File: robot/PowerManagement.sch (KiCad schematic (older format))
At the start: 13 parts

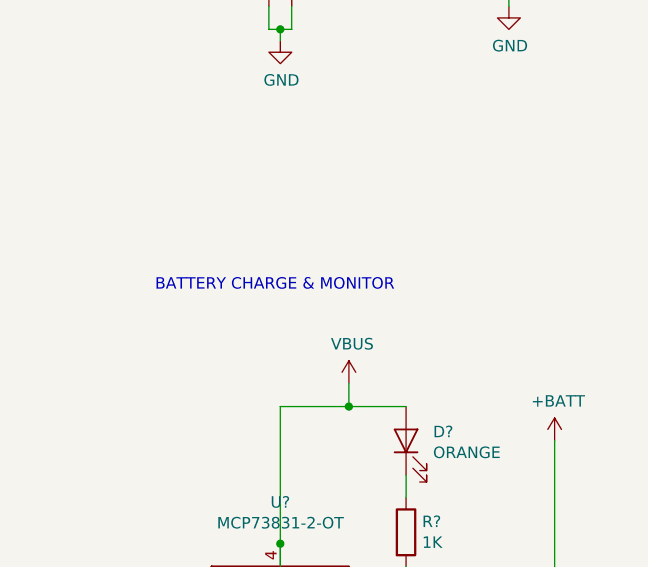
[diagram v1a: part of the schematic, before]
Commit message: UI parts, (re)wiring remaining signals
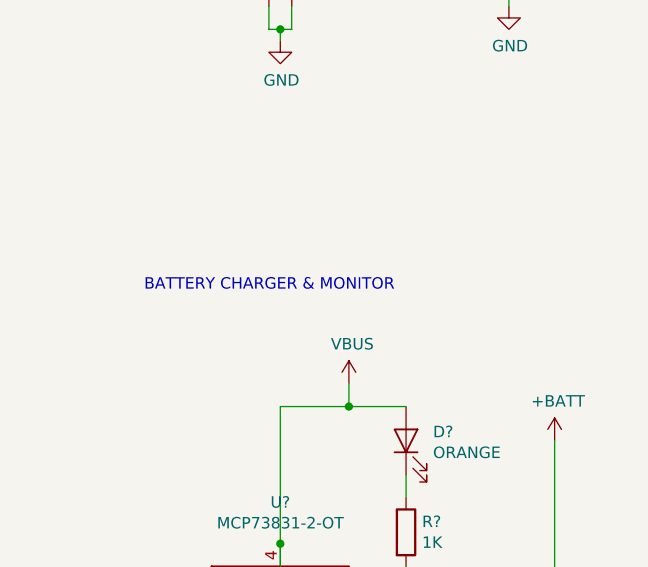
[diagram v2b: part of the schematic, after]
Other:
- note added: "BATTERY CHARGER & MONITOR"
- note removed: "BATTERY CHARGE & MONITOR"
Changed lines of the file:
@@
 $Descr A4 11693 8268
 encoding utf-8
-Sheet 2 7
+Sheet 2 8
 Title "Micro Sumo: Power Management"
 Date "2019-06-28"
@@
 BAT_MON
 Text Notes 3500 3850 2    50   ~ 0
-BATTERY CHARGE & MONITOR
+BATTERY CHARGER & MONITOR
 $Comp
 L dk_PMIC-Voltage-Regulators-Linear:LD1117S33CTR U?

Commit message: DRC check fixes and small changes
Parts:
- gave numbers to parts that had none: 13
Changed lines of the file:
@@
 $EndDescr
 $Comp
-L Battery_Management:MCP73831-2-OT U?
+L Battery_Management:MCP73831-2-OT U2
 U 1 1 5D163C93
 P 3000 5250
-F 0 "U?" H 3000 5731 50  0000 C CNN
+F 0 "U2" H 3000 5731 50  0000 C CNN
 F 1 "MCP73831-2-OT" H 3000 5640 50  0000 C CNN
 F 2 "Package_TO_SOT_SMD:SOT-23-5" H 3050 5000 50  0001 L CIN
@@
 $EndComp
 $Comp
-L Device:R R?
+L Device:R R4
 U 1 1 5D167CB7
 P 2500 5700
-F 0 "R?" H 2570 5746 50  0000 L CNN
+F 0 "R4" H 2570 5746 50  0000 L CNN
 F 1 "5K" H 2570 5655 50  0000 L CNN
 F 2 "" V 2430 5700 50  0001 C CNN
@@
 $EndComp
 $Comp
-L Device:C C?
+L Device:C C2
 U 1 1 5D16C2F0
 P 4200 5350
-F 0 "C?" H 4315 5396 50  0000 L CNN
+F 0 "C2" H 4315 5396 50  0000 L CNN
 F 1 "10µ" H 4315 5305 50  0000 L CNN
 F 2 "" H 4238 5200 50  0001 C CNN
@@
 	3300 4350 3300 4250
 $Comp
-L Device:LED D?
+L Device:LED D2
 U 1 1 5D16DD5D
 P 3550 4500
-F 0 "D?" V 3589 4382 50  0000 R CNN
+F 0 "D2" V 3589 4382 50  0000 R CNN
 F 1 "ORANGE" V 3498 4382 50  0000 R CNN
 F 2 "" H 3550 4500 50  0001 C CNN
@@
 Connection ~ 3300 4350
 $Comp
-L Device:R R?
+L Device:R R3
 U 1 1 5D170C73
 P 3550 4900
-F 0 "R?" H 3620 4946 50  0000 L CNN
+F 0 "R3" H 3620 4946 50  0000 L CNN
 F 1 "1K" H 3620 4855 50  0000 L CNN
 F 2 "" V 3480 4900 50  0001 C CNN
@@
 	3400 5150 4200 5150
 $Comp
-L Device:R R?
+L Device:R R1
 U 1 1 5D176A1F
 P 7650 1850
-F 0 "R?" H 7720 1896 50  0000 L CNN
+F 0 "R1" H 7720 1896 50  0000 L CNN
 F 1 "100K" H 7720 1805 50  0000 L CNN
 F 2 "" V 7580 1850 50  0001 C CNN
@@
 $EndComp
 $Comp
-L Device:R R?
+L Device:R R2
 U 1 1 5D176E0F
 P 7650 2350
-F 0 "R?" H 7720 2396 50  0000 L CNN
+F 0 "R2" H 7720 2396 50  0000 L CNN
 F 1 "100K" H 7720 2305 50  0000 L CNN
 F 2 "" V 7580 2350 50  0001 C CNN
@@
 BATTERY CHARGER & MONITOR
 $Comp
-L dk_PMIC-Voltage-Regulators-Linear:LD1117S33CTR U?
+L dk_PMIC-Voltage-Regulators-Linear:LD1117S33CTR U1
 U 1 1 5D1793ED
 P 2950 2200
-F 0 "U?" H 3000 2487 60  0000 C CNN
+F 0 "U1" H 3000 2487 60  0000 C CNN
 F 1 "LD1117S33CTR" H 3000 2381 60  0000 C CNN
 F 2 "digikey-footprints:SOT-223" H 3150 2400 60  0001 L CNN
@@
 $EndComp
 $Comp
-L Device:C C?
+L Device:C C1
 U 1 1 5D17BD3C
 P 4000 2400
-F 0 "C?" H 4115 2446 50  0000 L CNN
+F 0 "C1" H 4115 2446 50  0000 L CNN
 F 1 "10µ" H 4115 2355 50  0000 L CNN
 F 2 "" H 4038 2250 50  0001 C CNN
@@
 Connection ~ 4000 2200
 $Comp
-L Connector:TestPoint TP?
+L Connector:TestPoint TP1
 U 1 1 5D17DA83
 P 3550 2000
-F 0 "TP?" H 3608 2118 50  0000 L CNN
+F 0 "TP1" H 3608 2118 50  0000 L CNN
 F 1 "TestPoint" H 3608 2027 50  0000 L CNN
 F 2 "" H 3750 2000 50  0001 C CNN
@@
 $EndComp
 $Comp
-L Device:D_Schottky D?
+L Device:D_Schottky D1
 U 1 1 5D183802
 P 2350 1850
-F 0 "D?" V 2396 1771 50  0000 R CNN
+F 0 "D1" V 2396 1771 50  0000 R CNN
 F 1 "D_Schottky" V 2305 1771 50  0000 R CNN
 F 2 "" H 2350 1850 50  0001 C CNN
@@
 POWER SENSOR
 $Comp
-L Connector:Conn_01x02_Male J?
+L Connector:Conn_01x02_Male J1
 U 1 1 5D189E7A
 P 6800 4800
-F 0 "J?" H 6908 4981 50  0000 C CNN
+F 0 "J1" H 6908 4981 50  0000 C CNN
 F 1 "Conn_01x02_Male" H 6908 4890 50  0000 C CNN
 F 2 "" H 6800 4800 50  0001 C CNN
@@
 	7150 4900 7150 5050
 $Comp
-L Connector:USB_B_Micro J?
+L Connector:USB_B_Micro J2
 U 1 1 5D18EADA
 P 8050 4900
-F 0 "J?" H 8107 5367 50  0000 C CNN
+F 0 "J2" H 8107 5367 50  0000 C CNN
 F 1 "USB_B_Micro" H 8107 5276 50  0000 C CNN
 F 2 "" H 8200 4850 50  0001 C CNN

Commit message: Testpoints, switch, small changes
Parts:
- added SW1: SW_DPDT_x2, symbol Switch:SW_DPDT_x2
- added TP2, TP3: TestPoint, symbol Connector:TestPoint
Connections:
- net +BATT: now also SW1.1 (A), TP3.1; no longer D1.2 (A)
- net BAT_MON: now also TP2.1
- new net: D1.2 (A), SW1.2 (B)
- no-connect marks 1 -> 2
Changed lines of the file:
@@
 U 1 1 5D163C93
 P 3000 5250
-F 0 "U2" H 3000 5731 50  0000 C CNN
-F 1 "MCP73831-2-OT" H 3000 5640 50  0000 C CNN
+F 0 "U2" H 2700 5500 50  0000 C CNN
+F 1 "MCP73831-2-OT" H 3400 4950 50  0000 C CNN
 F 2 "Package_TO_SOT_SMD:SOT-23-5" H 3050 5000 50  0001 L CIN
 F 3 "http://ww1.microchip.com/downloads/en/DeviceDoc/20001984g.pdf" H 2850 5200 50  0001 C CNN
@@
 $EndComp
 $Comp
-L power:GND #PWR0101
+L power:GND #PWR015
 U 1 1 5D1650B8
 P 3000 6000
-F 0 "#PWR0101" H 3000 5750 50  0001 C CNN
+F 0 "#PWR015" H 3000 5750 50  0001 C CNN
 F 1 "GND" H 3005 5827 50  0000 C CNN
 F 2 "" H 3000 6000 50  0001 C CNN
@@
 $EndComp
 $Comp
-L power:VBUS #PWR0102
+L power:VBUS #PWR08
 U 1 1 5D1658D8
 P 3300 4250
-F 0 "#PWR0102" H 3300 4100 50  0001 C CNN
+F 0 "#PWR08" H 3300 4100 50  0001 C CNN
 F 1 "VBUS" H 3315 4423 50  0000 C CNN
 F 2 "" H 3300 4250 50  0001 C CNN
@@
 $EndComp
 $Comp
-L power:+BATT #PWR0103
+L power:+BATT #PWR09
 U 1 1 5D166644
 P 4200 4500
-F 0 "#PWR0103" H 4200 4350 50  0001 C CNN
+F 0 "#PWR09" H 4200 4350 50  0001 C CNN
 F 1 "+BATT" H 4215 4673 50  0000 C CNN
 F 2 "" H 4200 4500 50  0001 C CNN
@@
 	4200 5150 4200 4500
 $Comp
-L power:GND #PWR0104
+L power:GND #PWR014
 U 1 1 5D16B634
 P 4200 5550
-F 0 "#PWR0104" H 4200 5300 50  0001 C CNN
+F 0 "#PWR014" H 4200 5300 50  0001 C CNN
 F 1 "GND" H 4205 5377 50  0000 C CNN
 F 2 "" H 4200 5550 50  0001 C CNN
@@
 $EndComp
 $Comp
-L power:+BATT #PWR0105
+L power:+BATT #PWR02
 U 1 1 5D177175
 P 7650 1550
-F 0 "#PWR0105" H 7650 1400 50  0001 C CNN
+F 0 "#PWR02" H 7650 1400 50  0001 C CNN
 F 1 "+BATT" H 7665 1723 50  0000 C CNN
 F 2 "" H 7650 1550 50  0001 C CNN
@@
 $EndComp
 $Comp
-L power:GND #PWR0106
+L power:GND #PWR06
 U 1 1 5D177892
 P 7650 2650
-F 0 "#PWR0106" H 7650 2400 50  0001 C CNN
+F 0 "#PWR06" H 7650 2400 50  0001 C CNN
 F 1 "GND" H 7655 2477 50  0000 C CNN
 F 2 "" H 7650 2650 50  0001 C CNN
@@
 $EndComp
 $Comp
-L power:+3V3 #PWR0107
+L power:+3V3 #PWR03
 U 1 1 5D17A5F9
 P 4000 1850
-F 0 "#PWR0107" H 4000 1700 50  0001 C CNN
+F 0 "#PWR03" H 4000 1700 50  0001 C CNN
 F 1 "+3V3" H 4015 2023 50  0000 C CNN
 F 2 "" H 4000 1850 50  0001 C CNN
@@
 $EndComp
 $Comp
-L power:GND #PWR0108
+L power:GND #PWR05
 U 1 1 5D17AFB6
 P 4000 2600
-F 0 "#PWR0108" H 4000 2350 50  0001 C CNN
+F 0 "#PWR05" H 4000 2350 50  0001 C CNN
 F 1 "GND" H 4005 2427 50  0000 C CNN
 F 2 "" H 4000 2600 50  0001 C CNN
@@
 Connection ~ 3550 2200
 $Comp
-L power:GND #PWR0109
+L power:GND #PWR07
 U 1 1 5D1808D5
 P 3000 2750
-F 0 "#PWR0109" H 3000 2500 50  0001 C CNN
+F 0 "#PWR07" H 3000 2500 50  0001 C CNN
 F 1 "GND" H 3005 2577 50  0000 C CNN
 F 2 "" H 3000 2750 50  0001 C CNN
@@
 Connection ~ 3000 2700
 $Comp
-L power:+BATT #PWR0110
+L power:+BATT #PWR01
 U 1 1 5D18276E
-P 2350 1550
-F 0 "#PWR0110" H 2350 1400 50  0001 C CNN
-F 1 "+BATT" H 2365 1723 50  0000 C CNN
-F 2 "" H 2350 1550 50  0001 C CNN
-F 3 "" H 2350 1550 50  0001 C CNN
-	1    2350 1550
-	1    0    0    -1
-$EndComp
-$Comp
-L power:VBUS #PWR0111
+P 2250 950
+F 0 "#PWR01" H 2250 800 50  0001 C CNN
+F 1 "+BATT" H 2265 1123 50  0000 C CNN
+F 2 "" H 2250 950 50  0001 C CNN
+F 3 "" H 2250 950 50  0001 C CNN
+	1    2250 950
+	1    0    0    -1
+$EndComp
+$Comp
+L power:VBUS #PWR04
 U 1 1 5D182F66
 P 1950 2050
-F 0 "#PWR0111" H 1950 1900 50  0001 C CNN
+F 0 "#PWR04" H 1950 1900 50  0001 C CNN
 F 1 "VBUS" H 1965 2223 50  0000 C CNN
 F 2 "" H 1950 2050 50  0001 C CNN
@@
 	1950 2200 2350 2200
 Wire Wire Line
-	2350 1550 2350 1700
-Wire Wire Line
 	2350 2000 2350 2200
 Connection ~ 2350 2200
 Wire Wire Line
 	2350 2200 2550 2200
-Text Notes 3550 1150 2    50   ~ 0
+Text Notes 3350 600  2    50   ~ 0
 POWER CONVERTOR
 Text Notes 8000 1150 2    50   ~ 0
@@
 U 1 1 5D189E7A
 P 6800 4800
-F 0 "J1" H 6908 4981 50  0000 C CNN
-F 1 "Conn_01x02_Male" H 6908 4890 50  0000 C CNN
+F 0 "J1" H 6800 4950 50  0000 C CNN
+F 1 "Conn_01x02_Male" H 6750 4600 50  0000 C CNN
 F 2 "" H 6800 4800 50  0001 C CNN
 F 3 "~" H 6800 4800 50  0001 C CNN
@@
 $EndComp
 $Comp
-L power:GND #PWR0112
+L power:GND #PWR012
 U 1 1 5D18ADA8
 P 7150 5050
-F 0 "#PWR0112" H 7150 4800 50  0001 C CNN
+F 0 "#PWR012" H 7150 4800 50  0001 C CNN
 F 1 "GND" H 7155 4877 50  0000 C CNN
 F 2 "" H 7150 5050 50  0001 C CNN
@@
 $EndComp
 $Comp
-L power:+BATT #PWR0113
+L power:+BATT #PWR011
 U 1 1 5D18B140
 P 7150 4650
-F 0 "#PWR0113" H 7150 4500 50  0001 C CNN
+F 0 "#PWR011" H 7150 4500 50  0001 C CNN
 F 1 "+BATT" H 7165 4823 50  0000 C CNN
 F 2 "" H 7150 4650 50  0001 C CNN
@@
 U 1 1 5D18EADA
 P 8050 4900
-F 0 "J2" H 8107 5367 50  0000 C CNN
-F 1 "USB_B_Micro" H 8107 5276 50  0000 C CNN
+F 0 "J2" H 8050 5350 50  0000 C CNN
+F 1 "USB_B_Micro" H 8050 5250 50  0000 C CNN
 F 2 "" H 8200 4850 50  0001 C CNN
 F 3 "~" H 8200 4850 50  0001 C CNN
@@
 $EndComp
 $Comp
-L power:VBUS #PWR0114
+L power:VBUS #PWR010
 U 1 1 5D19110E
 P 8500 4550
-F 0 "#PWR0114" H 8500 4400 50  0001 C CNN
+F 0 "#PWR010" H 8500 4400 50  0001 C CNN
 F 1 "VBUS" H 8515 4723 50  0000 C CNN
 F 2 "" H 8500 4550 50  0001 C CNN
@@
 $EndComp
 $Comp
-L power:GND #PWR0115
+L power:GND #PWR013
 U 1 1 5D1917C1
 P 8000 5400
-F 0 "#PWR0115" H 8000 5150 50  0001 C CNN
+F 0 "#PWR013" H 8000 5150 50  0001 C CNN
 F 1 "GND" H 8005 5227 50  0000 C CNN
 F 2 "" H 8000 5400 50  0001 C CNN
@@
 Text Notes 8000 3950 2    50   ~ 0
 POWER CONNECTORS
+$Comp
+L Connector:TestPoint TP3
+U 1 1 5D777CE8
+P 4500 5100
+F 0 "TP3" H 4558 5218 50  0000 L CNN
+F 1 "TestPoint" H 4558 5127 50  0000 L CNN
+F 2 "" H 4700 5100 50  0001 C CNN
+F 3 "~" H 4700 5100 50  0001 C CNN
+	1    4500 5100
+	1    0    0    -1
+$EndComp
+$Comp
+L Connector:TestPoint TP2
+U 1 1 5D779FBE
+P 7050 2050
+F 0 "TP2" H 7108 2168 50  0000 L CNN
+F 1 "TestPoint" H 7108 2077 50  0000 L CNN
+F 2 "" H 7250 2050 50  0001 C CNN
+F 3 "~" H 7250 2050 50  0001 C CNN
+	1    7050 2050
+	1    0    0    -1
+$EndComp
+Wire Wire Line
+	7050 2100 7650 2100
+Wire Wire Line
+	4500 5150 4500 5100
+Wire Wire Line
+	4200 5150 4500 5150
+Wire Wire Line
+	7050 2050 7050 2100
+NoConn ~ 2450 1050
+Wire Wire Line
+	2350 1450 2350 1700
+$Comp
+L Switch:SW_DPDT_x2 SW1
+U 1 1 5D7A8209
+P 2350 1250
+F 0 "SW1" V 2396 1062 50  0000 R CNN
+F 1 "SW_DPDT_x2" V 2305 1062 50  0000 R CNN
+F 2 "" H 2350 1250 50  0001 C CNN
+F 3 "~" H 2350 1250 50  0001 C CNN
+	1    2350 1250
+	0    -1   -1   0
+$EndComp
+Wire Wire Line
+	2250 950  2250 1050
 $EndSCHEMATC
